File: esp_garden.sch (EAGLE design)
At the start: 31 parts, among them T1 DMN6068SE-13, T2 DMN6068SE-13, T3 DMN6068SE-13, T4 DMN6068SE-13, U1 V1, U10 V1, U11 V1, U12 V1, U13 V1, U14 V1, U15 V1, U2 V1, U3 V1, U4 V1, U5 V1, U6 V1, U7 V1, U8 V1, U9 V1

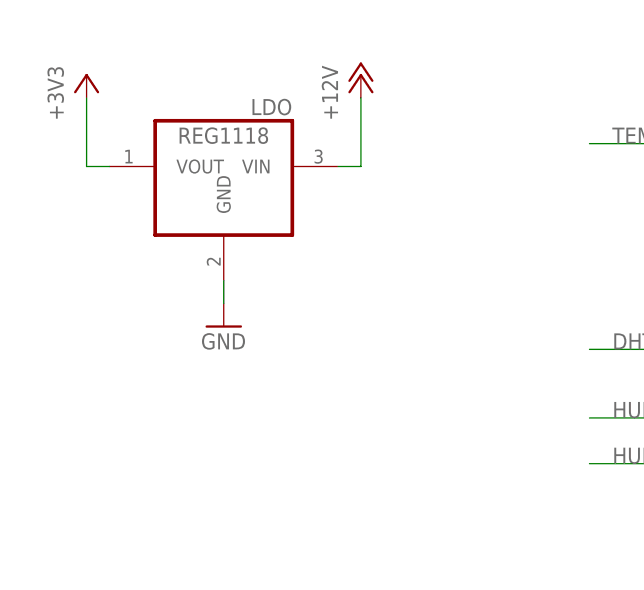
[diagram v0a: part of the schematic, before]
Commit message: Isolate for planes set to 0.254, added caps at LDO
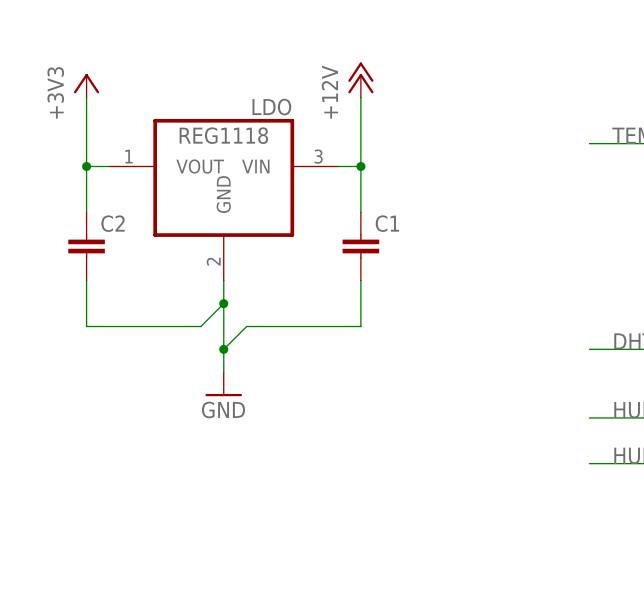
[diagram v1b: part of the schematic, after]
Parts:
- added C1, C2: (no value), rcl:C-EUC0805
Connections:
- net +12V: now also C1.1
- net +3V3: now also C2.1
- net GND: now also C1.2, C2.2
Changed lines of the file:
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@@
 <part name="P+2" library="supply1" deviceset="+12V" device=""/>
 <part name="U15" library="JKW_CHIP" deviceset="2_PIN_CONNECTOR" device="" value="V1"/>
+<part name="C1" library="rcl" deviceset="C-EU" device="C0805"/>
+<part name="C2" library="rcl" deviceset="C-EU" device="C0805"/>
 </parts>
 <sheets>
@@
 <attribute name="NAME" x="209.042" y="57.912" size="1.778" layer="95" rot="R90"/>
 </instance>
-<instance part="GND4" gate="1" x="10.16" y="68.58"/>
+<instance part="GND4" gate="1" x="10.16" y="60.96"/>
 <instance part="U4" gate="G$1" x="200.66" y="81.28" smashed="yes">
 <attribute name="NAME" x="209.042" y="80.772" size="1.778" layer="95" rot="R90"/>
@@
 <attribute name="NAME" x="87.122" y="22.352" size="1.778" layer="95" rot="R90"/>
 </instance>
+<instance part="C1" gate="G$1" x="25.4" y="78.74"/>
+<instance part="C2" gate="G$1" x="-5.08" y="78.74"/>
 </instances>
 <busses>
@@
 <pinref part="LDO" gate="G$1" pin="GND"/>
 <pinref part="GND4" gate="1" pin="GND"/>
+<wire x1="10.16" y1="63.5" x2="10.16" y2="66.04" width="0.1524" layer="91"/>
+<wire x1="10.16" y1="66.04" x2="10.16" y2="71.12" width="0.1524" layer="91"/>
+<pinref part="C1" gate="G$1" pin="2"/>
 <wire x1="10.16" y1="71.12" x2="10.16" y2="73.66" width="0.1524" layer="91"/>
+<wire x1="25.4" y1="73.66" x2="25.4" y2="68.58" width="0.1524" layer="91"/>
+<wire x1="25.4" y1="68.58" x2="12.7" y2="68.58" width="0.1524" layer="91"/>
+<wire x1="12.7" y1="68.58" x2="10.16" y2="66.04" width="0.1524" layer="91"/>
+<junction x="10.16" y="66.04"/>
+<pinref part="C2" gate="G$1" pin="2"/>
+<wire x1="-5.08" y1="73.66" x2="-5.08" y2="68.58" width="0.1524" layer="91"/>
+<wire x1="-5.08" y1="68.58" x2="7.62" y2="68.58" width="0.1524" layer="91"/>
+<wire x1="7.62" y1="68.58" x2="10.16" y2="71.12" width="0.1524" layer="91"/>
+<junction x="10.16" y="71.12"/>
 </segment>
 <segment>
@@
 <wire x1="22.86" y1="86.36" x2="25.4" y2="86.36" width="0.1524" layer="91"/>
 <wire x1="25.4" y1="86.36" x2="25.4" y2="93.98" width="0.1524" layer="91"/>
+<pinref part="C1" gate="G$1" pin="1"/>
+<wire x1="25.4" y1="86.36" x2="25.4" y2="81.28" width="0.1524" layer="91"/>
+<junction x="25.4" y="86.36"/>
 </segment>
 <segment>
@@
 <pinref part="LDO" gate="G$1" pin="VOUT"/>
 <wire x1="-5.08" y1="86.36" x2="-2.54" y2="86.36" width="0.1524" layer="91"/>
-</segment>
-<segment>
+<pinref part="C2" gate="G$1" pin="1"/>
+<wire x1="-5.08" y1="86.36" x2="-5.08" y2="81.28" width="0.1524" layer="91"/>
+<junction x="-5.08" y="86.36"/>
+</segment>
+<segment>

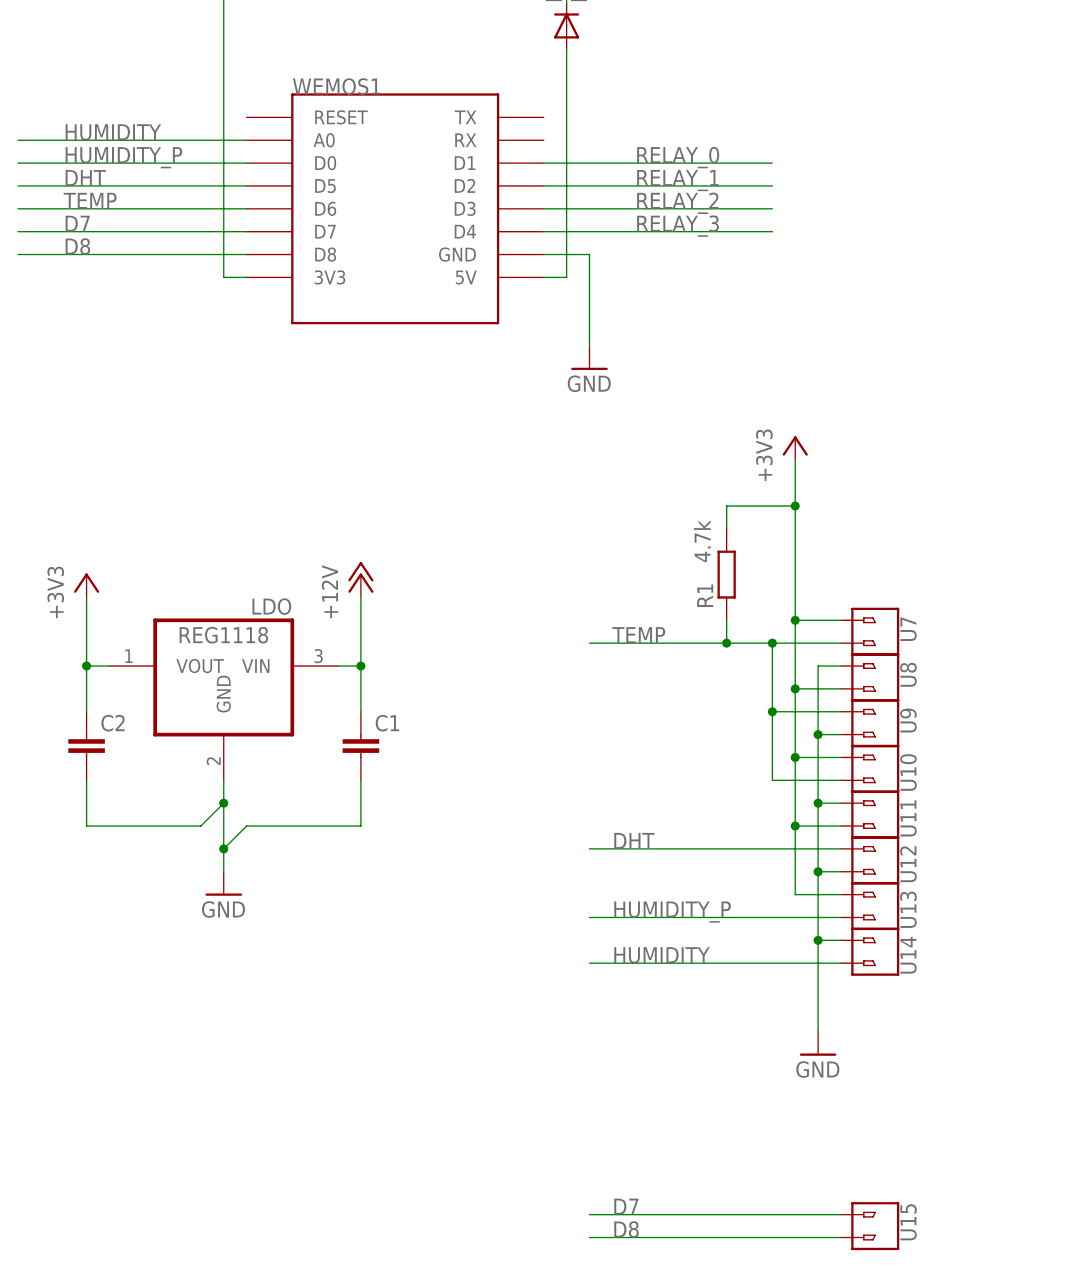
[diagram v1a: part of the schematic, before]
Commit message: Added support for I2C sensor, changed LDO to REG1117
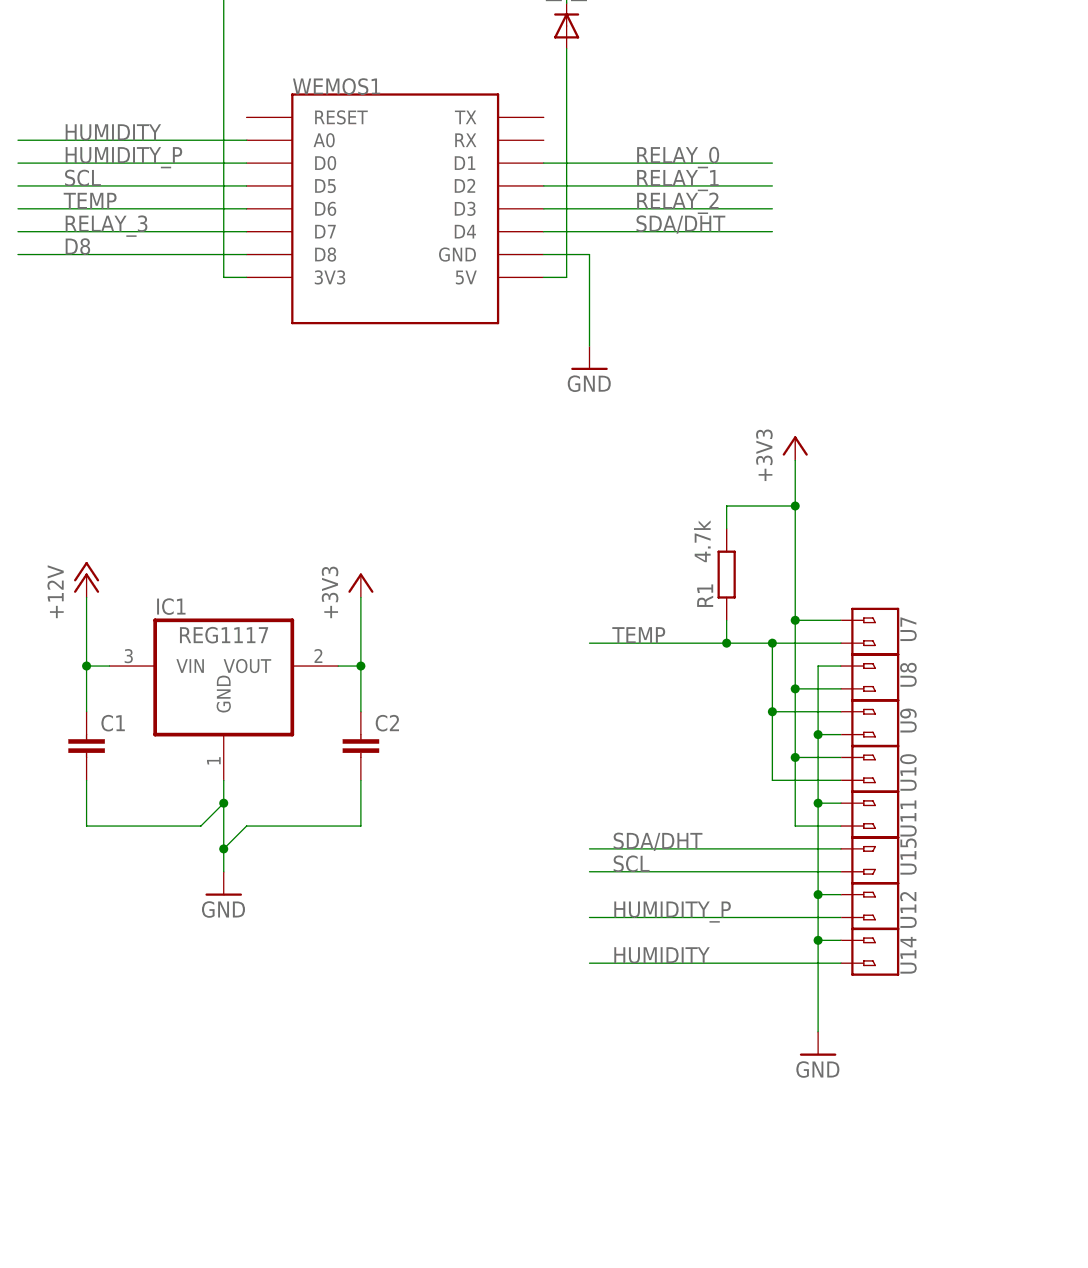
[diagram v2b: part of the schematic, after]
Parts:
- removed LDO: REG1118, burr-brown:REG1118
- removed U13: V1, JKW_CHIP:2_PIN_CONNECTOR
- added IC1: REG1117, burr-brown:REG1117
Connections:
- removed net D7: U15.1, WEMOS1.D7
- removed net DHT: U12.2, WEMOS1.D5
- new net SCL: U15.2, WEMOS1.D5
- new net SDA/DHT: U15.1, WEMOS1.D4
- net +12V: now also IC1.VIN; no longer LDO.VIN
- net +3V3: now also IC1.VOUT; no longer LDO.VOUT, U13.2
- net D8: no longer U15.2
- net GND: now also IC1.GND, U12.2; no longer LDO.GND, U12.1
- net HUMIDITY_P: now also U12.1; no longer U13.1
- net RELAY_3: now also WEMOS1.D7; no longer WEMOS1.D4
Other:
- moved on the sheet: C1, C2, U12, U15

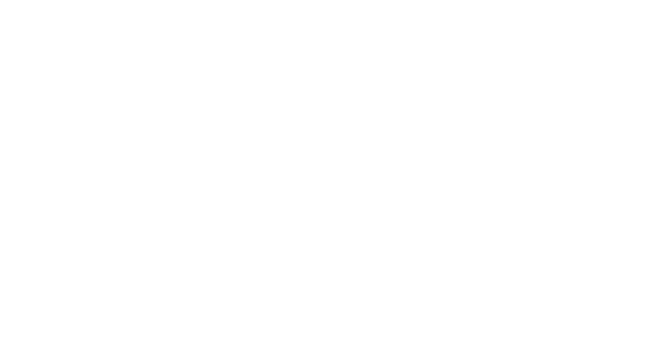
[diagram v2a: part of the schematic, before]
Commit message: Added text on PCB
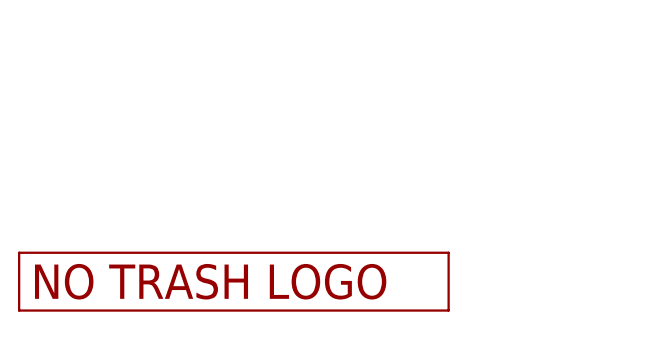
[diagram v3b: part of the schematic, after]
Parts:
- added U$1: LOGO_NO_TRASHNO_TRASH, JKW_CHIP:LOGO_NO_TRASHNO_TRASH
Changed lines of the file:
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@@
 <part name="C2" library="rcl" deviceset="C-EU" device="C0805"/>
 <part name="IC1" library="burr-brown" deviceset="REG1117" device=""/>
+<part name="U$1" library="JKW_CHIP" deviceset="LOGO_NO_TRASH" device="NO_TRASH"/>
 </parts>
 <sheets>
@@
 <instance part="C2" gate="G$1" x="25.4" y="78.74"/>
 <instance part="IC1" gate="G$1" x="10.16" y="86.36"/>
+<instance part="U$1" gate="G$1" x="-25.4" y="2.54"/>
 </instances>
 <busses>

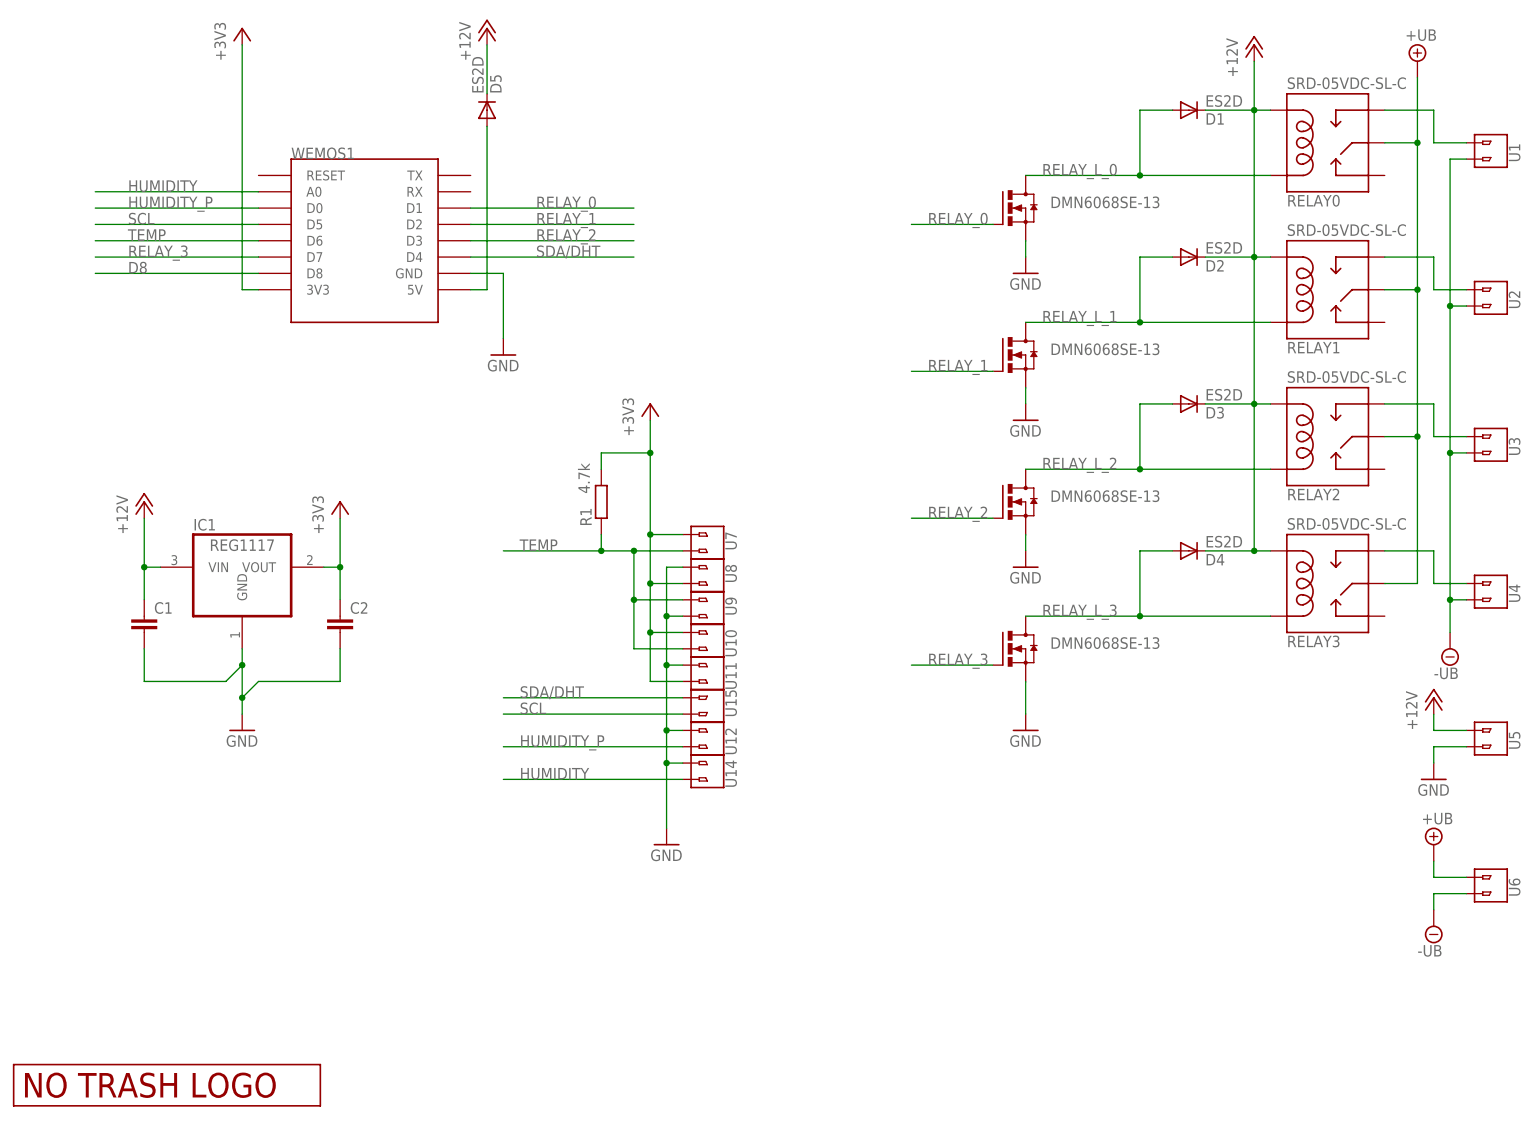
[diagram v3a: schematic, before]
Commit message: added options for DHT22 onboard and special use for relais 0
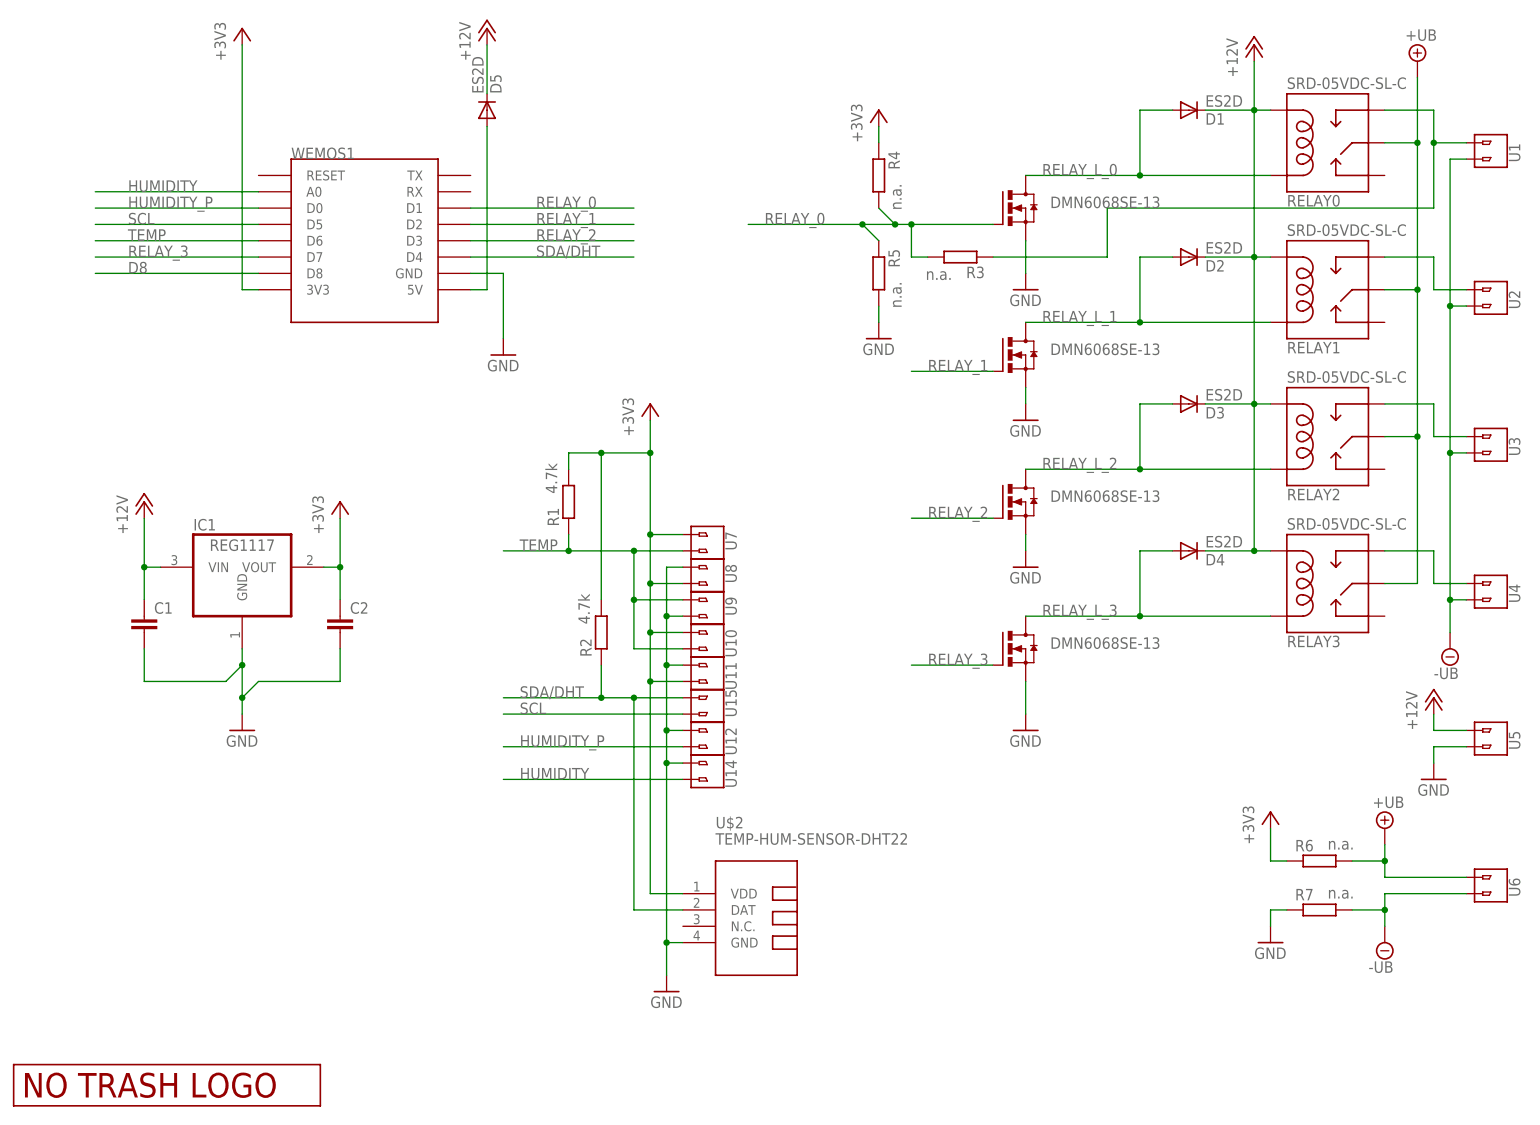
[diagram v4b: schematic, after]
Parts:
- added R2: 4.7k, rcl:R-EU_M0805
- added R3, R4, R5, R6, R7: n.a., rcl:R-EU_M0805
- added U$2: TEMP-HUM-SENSOR-DHT22, diy-modules:TEMP-HUM-SENSOR-DHT22
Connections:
- net +3V3: now also R2.2, R4.1, R6.1, U$2.VDD
- net +UB: now also R6.2
- net -UB: now also R7.2
- net GND: now also R5.2, R7.1, U$2.GND
- net N$4: now also R3.1
- net RELAY_0: now also R3.2, R4.2, R5.1
- net SDA/DHT: now also R2.1, U$2.DAT
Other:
- moved on the sheet: R1
